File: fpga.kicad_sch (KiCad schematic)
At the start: 44 parts, among them Q1 Q_NPN_BCE, U3 ICE40HX4K-TQ144, U6 TLV70012_SOT23-5

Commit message: Oops, no, _this_ is v1.0
;-)
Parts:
- R16: value 4k7 -> 4K7
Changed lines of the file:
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@@
       (effects (font (size 1.27 1.27)) (justify left))
     )
-    (property "Value" "4k7" (id 1) (at 199.39 119.3799 0)
+    (property "Value" "4K7" (id 1) (at 199.39 119.3799 0)
       (effects (font (size 1.27 1.27)) (justify left))
     )

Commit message: v2: ADV7513 and FFC
Large work much progress - almost routed
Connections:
- net ALT_VID_I2S_CLK: now also U3.143 (IOT_221); no longer U3.144 (IOT_222)
- net ALT_VID_I2S_DATA: now also U3.144 (IOT_222); no longer U3.142 (IOT_220)
- net ALT_VID_I2S_WS: now also U3.142 (IOT_220); no longer U3.143 (IOT_221)
- net RGB0: now also U3.4 (IOL_3B); no longer U3.25 (IOL_18A)
- net RGB1: now also U3.7 (IOL_4A); no longer U3.26 (IOL_18B)
- net RGB10: now also U3.19 (IOL_13A); no longer U3.18 (IOL_12B)
- net RGB11: now also U3.20 (IOL_13B_GBIN7); no longer U3.19 (IOL_13A)
- net RGB16: now also U3.25 (IOL_18A); no longer U3.4 (IOL_3B)
- net RGB17: now also U3.26 (IOL_18B); no longer U3.7 (IOL_4A)
- net RGB18: now also U3.28 (IOL_23A); no longer U3.8 (IOL_4B)
- net RGB19: now also U3.29 (IOL_23B); no longer U3.9 (IOL_5A)
- net RGB2: now also U3.8 (IOL_4B); no longer U3.28 (IOL_23A)
- net RGB20: now also U3.31 (IOL_24A); no longer U3.10 (IOL_5B)
- net RGB21: now also U3.32 (IOL_24B); no longer U3.11 (IOL_8A)
- net RGB22: now also U3.33 (IOL_25A); no longer U3.12 (IOL_8B)
- net RGB23: now also U3.34 (IOL_25B); no longer U3.15 (IOL_10A)
- net RGB3: now also U3.9 (IOL_5A); no longer U3.29 (IOL_23B)
- net RGB4: now also U3.10 (IOL_5B); no longer U3.31 (IOL_24A)
- net RGB5: now also U3.11 (IOL_8A); no longer U3.32 (IOL_24B)
- net RGB6: now also U3.12 (IOL_8B); no longer U3.33 (IOL_25A)
- net RGB7: now also U3.15 (IOL_10A); no longer U3.34 (IOL_25B)
- net RGB9: now also U3.18 (IOL_12B); no longer U3.17 (IOL_12A)
- net VCKIN: now also U3.120 (IOT_179); no longer U3.93 (IOR_140_GBIN3)
- net VD0: now also U3.73 (IOR_109); no longer U3.104 (IOR_164)
- net VD1: now also U3.74 (IOR_110); no longer U3.105 (IOR_165)
- net VD10: now also U3.84 (IOR_120); no longer U3.117 (IOT_174)
- net VD11: now also U3.85 (IOR_128); no longer U3.118 (IOT_177)
- net VD12: now also U3.87 (IOR_136); no longer U3.119 (IOT_178)
- net VD13: now also U3.88 (IOR_137); no longer U3.120 (IOT_179)
- net VD14: now also U3.90 (IOR_138); no longer U3.121 (IOT_181)
- net VD15: now also U3.91 (IOR_139); no longer U3.122 (IOT_190)
- net VD16: now also U3.93 (IOR_140_GBIN3); no longer U3.82 (IOR_118)
- net VD17: now also U3.94 (IOR_141_GBIN2); no longer U3.83 (IOR_119)
- net VD18: now also U3.95 (IOR_144); no longer U3.84 (IOR_120)
- net VD19: now also U3.96 (IOR_146); no longer U3.85 (IOR_128)
- net VD2: now also U3.75 (IOR_111); no longer U3.106 (IOR_166)
- net VD20: now also U3.97 (IOR_147); no longer U3.87 (IOR_136)
- net VD21: now also U3.98 (IOR_148); no longer U3.88 (IOR_137)
- net VD22: now also U3.99 (IOR_152); no longer U3.90 (IOR_138)
- net VD23: now also U3.101 (IOR_160); no longer U3.91 (IOR_139)
- net VD24: now also U3.102 (IOR_161); no longer U3.94 (IOR_141_GBIN2)
- net VD25: now also U3.104 (IOR_164); no longer U3.95 (IOR_144)
- net VD26: now also U3.105 (IOR_165); no longer U3.96 (IOR_146)
- net VD27: now also U3.106 (IOR_166); no longer U3.97 (IOR_147)
- net VD28: now also U3.107 (IOR_167); no longer U3.98 (IOR_148)
- net VD29: now also U3.110 (IOT_168); no longer U3.99 (IOR_152)
- net VD3: now also U3.76 (IOR_112); no longer U3.107 (IOR_167)
- net VD30: now also U3.112 (IOT_169); no longer U3.101 (IOR_160)
- net VD31: now also U3.113 (IOT_170); no longer U3.102 (IOR_161)
- net VD4: now also U3.78 (IOR_114); no longer U3.110 (IOT_168)
- net VD5: now also U3.79 (IOR_115); no longer U3.112 (IOT_169)
- net VD6: now also U3.80 (IOR_116); no longer U3.113 (IOT_170)
- net VD7: now also U3.81 (IOR_117); no longer U3.114 (IOT_171)
- net VD8: now also U3.82 (IOR_118); no longer U3.115 (IOT_172)
- net VD9: now also U3.83 (IOR_119); no longer U3.116 (IOT_173)
- net VFLYBK: now also U3.119 (IOT_178); no longer U3.75 (IOR_111)
- net VID_OUT_HS: now also U3.2 (IOL_2B); no longer U3.1 (IOL_2A)
- net VID_OUT_PCLK: now also U3.17 (IOL_12A); no longer U3.20 (IOL_13B_GBIN7)
- net VID_OUT_VS: now also U3.1 (IOL_2A); no longer U3.2 (IOL_2B)
- net VSNDAK: now also U3.122 (IOT_190); no longer U3.74 (IOR_110)
- net VVIDAK: now also U3.121 (IOT_181); no longer U3.73 (IOR_109)
- net VnHS: now also U3.115 (IOT_172); no longer U3.79 (IOR_115)
- net VnSNDRQ: now also U3.118 (IOT_177); no longer U3.76 (IOR_112)
- net VnVCS: now also U3.116 (IOT_173); no longer U3.80 (IOR_116)
- net VnVIDRQ: now also U3.117 (IOT_174); no longer U3.78 (IOR_114)
- net VnVIDW: now also U3.114 (IOT_171); no longer U3.81 (IOR_117)
- net VID_CEC_CLK: now reaches U3.38 (IOB_57)

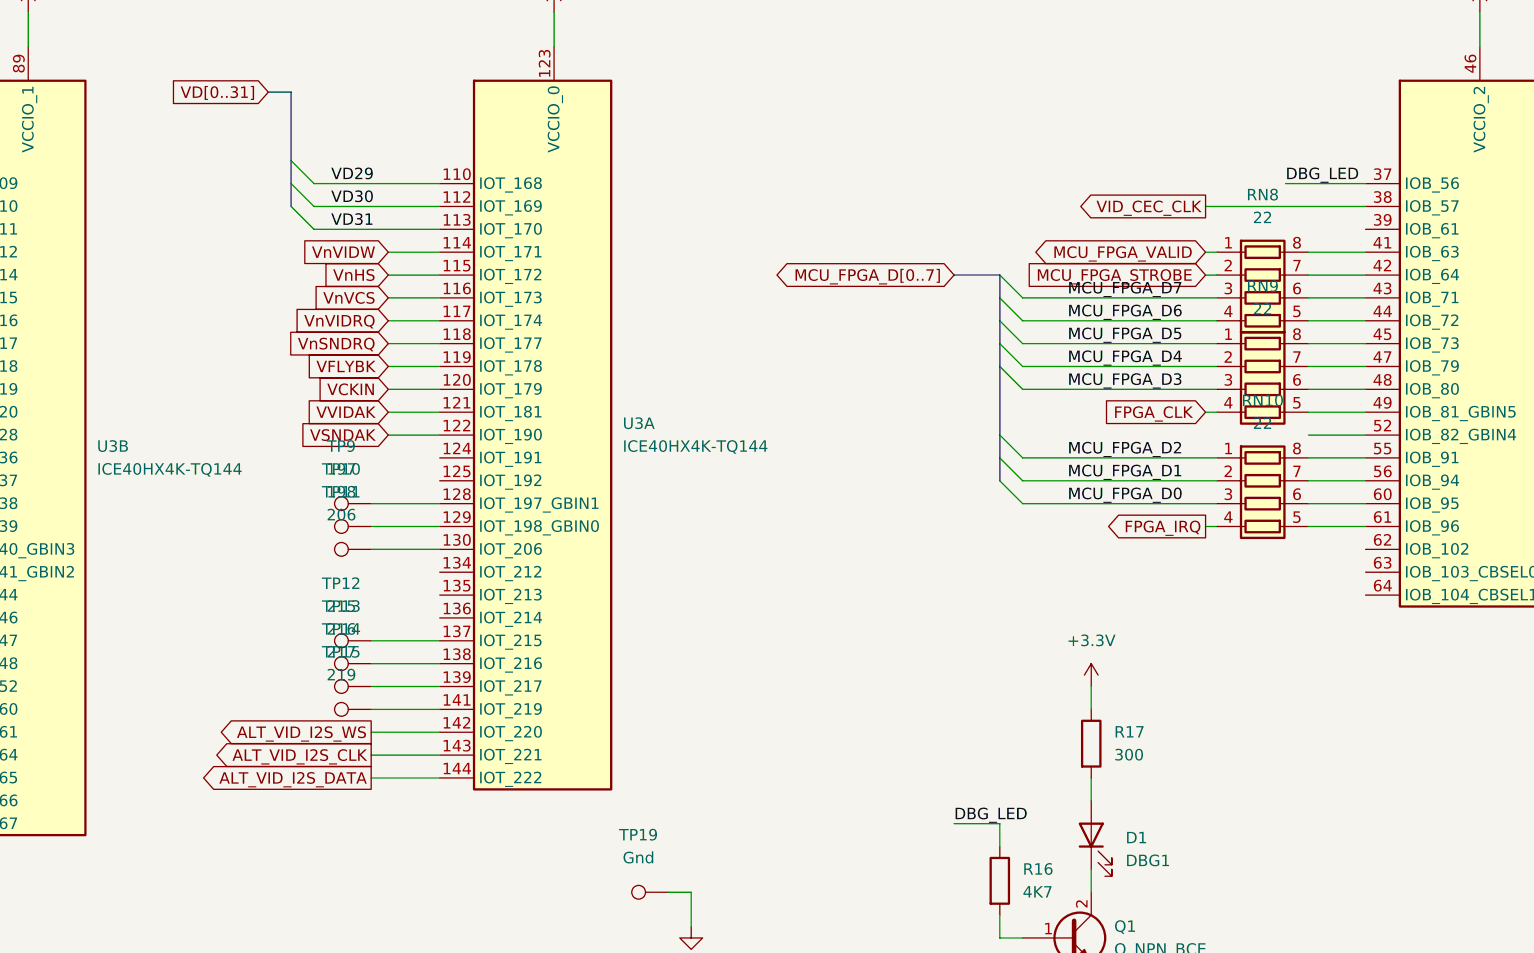
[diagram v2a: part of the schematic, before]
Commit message: 2.0 candiate: routed, looks neat, passes DRC
DVI differential pairs aren't tuned that nicely, but 'probs ok'
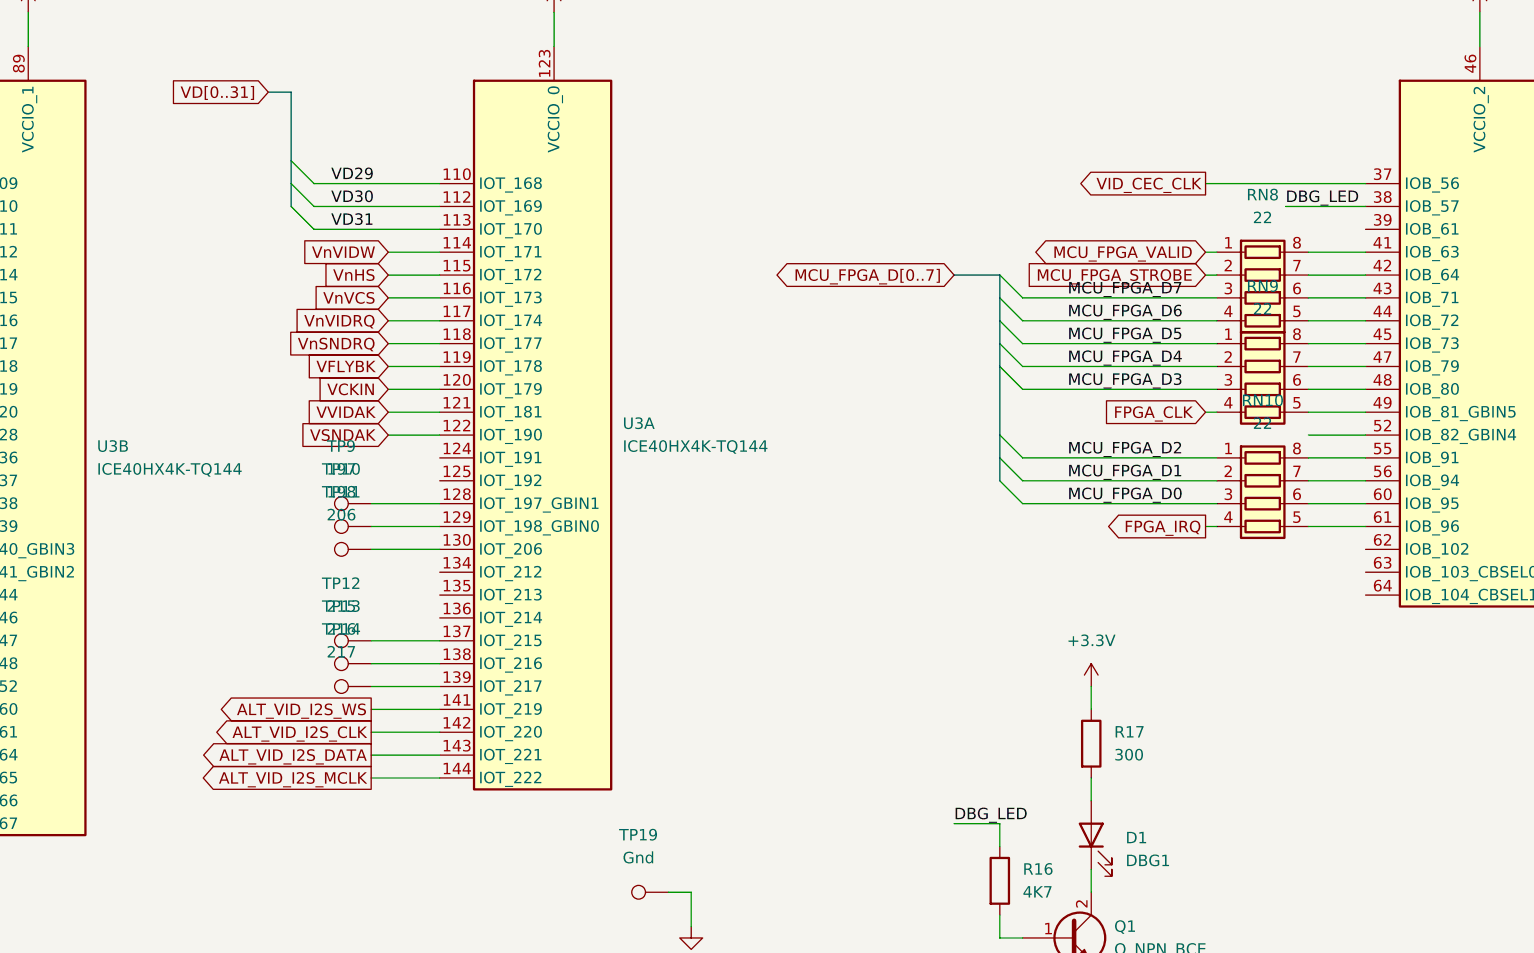
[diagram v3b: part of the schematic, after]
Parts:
- removed TP15: 219, TestPoint:TestPoint_Pad_D1.0mm, symbol Connector:TestPoint
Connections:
- net ALT_VID_I2S_CLK: now also U3.142 (IOT_220); no longer U3.143 (IOT_221)
- net ALT_VID_I2S_DATA: now also U3.143 (IOT_221); no longer U3.144 (IOT_222)
- net ALT_VID_I2S_WS: now also U3.141 (IOT_219); no longer U3.142 (IOT_220)
- net DBG_LED: now also U3.38 (IOB_57); no longer U3.37 (IOB_56)
- net VID_CEC_CLK: now also U3.37 (IOB_56); no longer U3.38 (IOB_57)
- new net ALT_VID_I2S_MCLK: U3.144 (IOT_222)
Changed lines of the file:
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@@
-    (stroke (width 0) (type default) (color 0 0 0 0))
-  )
-  (wire (pts (xy 219.71 43.18) (xy 237.49 43.18))
     (stroke (width 0) (type default) (color 0 0 0 0))
   )
@@
     (stroke (width 0) (type default) (color 0 0 0 0))
   )
+  (wire (pts (xy 228.6 43.18) (xy 237.49 43.18))
+    (stroke (width 0) (type default) (color 0 0 0 0))
+  )
   (wire (pts (xy 88.9 21.59) (xy 88.9 25.4))
     (stroke (width 0) (type default) (color 0 0 0 0))
@@
     (stroke (width 0) (type default) (color 0 0 0 0))
   )
-  (wire (pts (xy 228.6 40.64) (xy 237.49 40.64))
+  (wire (pts (xy 219.71 40.64) (xy 237.49 40.64))
     (stroke (width 0) (type default) (color 0 0 0 0))
   )
@@
     (effects (font (size 1.27 1.27)) (justify left bottom))
   )
-  (label "DBG_LED" (at 228.6 40.64 0)
+  (label "DBG_LED" (at 228.6 43.18 0)
     (effects (font (size 1.27 1.27)) (justify left bottom))
   )
@@
     )
   )
-  (global_label "ALT_VID_I2S_DATA" (shape output) (at 127 106.68 180) (fields_autoplaced)
-    (effects (font (size 1.27 1.27)) (justify right))
-    (property "Intersheet References" "${INTERSHEET_REFS}" (id 0) (at 108.1979 106.6006 0)
+  (global_label "ALT_VID_I2S_DATA" (shape output) (at 127 104.14 180) (fields_autoplaced)
+    (effects (font (size 1.27 1.27)) (justify right))
+    (property "Intersheet References" "${INTERSHEET_REFS}" (id 0) (at 108.1979 104.0606 0)
       (effects (font (size 1.27 1.27)) (justify right) hide)
     )
@@
     )
   )
-  (global_label "VID_CEC_CLK" (shape output) (at 219.71 43.18 180) (fields_autoplaced)
-    (effects (font (size 1.27 1.27)) (justify right))
-    (property "Intersheet References" "${INTERSHEET_REFS}" (id 0) (at 205.1412 43.1006 0)
-      (effects (font (size 1.27 1.27)) (justify right) hide)
-    )
-  )
-  (global_label "ALT_VID_I2S_CLK" (shape output) (at 127 104.14 180) (fields_autoplaced)
-    (effects (font (size 1.27 1.27)) (justify right))
-    (property "Intersheet References" "${INTERSHEET_REFS}" (id 0) (at 109.0445 104.0606 0)
+  (global_label "VID_CEC_CLK" (shape output) (at 219.71 40.64 180) (fields_autoplaced)
+    (effects (font (size 1.27 1.27)) (justify right))
+    (property "Intersheet References" "${INTERSHEET_REFS}" (id 0) (at 205.1412 40.5606 0)
+      (effects (font (size 1.27 1.27)) (justify right) hide)
+    )
+  )
+  (global_label "ALT_VID_I2S_CLK" (shape output) (at 127 101.6 180) (fields_autoplaced)
+    (effects (font (size 1.27 1.27)) (justify right))
+    (property "Intersheet References" "${INTERSHEET_REFS}" (id 0) (at 109.0445 101.5206 0)
       (effects (font (size 1.27 1.27)) (justify right) hide)
     )
@@
     )
   )
+  (global_label "ALT_VID_I2S_MCLK" (shape output) (at 127 106.68 180) (fields_autoplaced)
+    (effects (font (size 1.27 1.27)) (justify right))
+    (property "Intersheet References" "${INTERSHEET_REFS}" (id 0) (at 107.5931 106.6006 0)
+      (effects (font (size 1.27 1.27)) (justify right) hide)
+    )
+  )
   (global_label "FPGA_SPI_DOUT" (shape output) (at 46.99 219.71 180) (fields_autoplaced)
     (effects (font (size 1.27 1.27)) (justify right))
@@
     )
   )
-  (global_label "ALT_VID_I2S_WS" (shape output) (at 127 101.6 180) (fields_autoplaced)
-    (effects (font (size 1.27 1.27)) (justify right))
-    (property "Intersheet References" "${INTERSHEET_REFS}" (id 0) (at 109.9517 101.5206 0)
+  (global_label "ALT_VID_I2S_WS" (shape output) (at 127 99.06 180) (fields_autoplaced)
+    (effects (font (size 1.27 1.27)) (justify right))
+    (property "Intersheet References" "${INTERSHEET_REFS}" (id 0) (at 109.9517 98.9806 0)
       (effects (font (size 1.27 1.27)) (justify right) hide)
     )
@@
       (effects (font (size 1.27 1.27)) hide)
     )
-    (pin "1")
-  )
-  (symbol (lib_id "Connector:TestPoint") (at 127 99.06 90) (unit 1)
-    (in_bom yes) (on_board yes) (fields_autoplaced)
-    (property "Reference" "TP15" (id 0) (at 123.698 92.71 90))
-    (property "Value" "219" (id 1) (at 123.698 95.25 90))
-    (property "Footprint" "TestPoint:TestPoint_Pad_D1.0mm" (id 2) (at 127 93.98 0)
-      (effects (font (size 1.27 1.27)) hide)
-    )
-    (property "Datasheet" "~" (id 3) (at 127 93.98 0)
-      (effects (font (size 1.27 1.27)) hide)
-    )
